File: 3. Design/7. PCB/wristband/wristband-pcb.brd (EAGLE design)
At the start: 160 x 100 mm, 44 parts, among them IC2 MAX16150AUT+T, IC5 STM32F051K6U6, Q1 2N7002NXAKR, Y2 FA-20H_16.0000MF12Z-AC3, Y3 FA-20H_16.0000MF12Z-AC3

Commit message: ADD|UPDT: Finished presentation
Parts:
- moved Y3 78.1 mm to (11.9, 13.0)
- moved BATT_HLD 67.4 mm to (13.1, 9.78), flipped to the bottom
- moved NRF24L01+ 63.8 mm to (12.7, 24.1)
- moved IC5 50.0 mm to (21.6, 22.9)
- moved PROG_IF 35.2 mm to (19.1, 40.9)
- moved MPU_6050_IF 29.7 mm to (29.8, 6.99)
- moved C11 16.5 mm to (42.8, 69.8)
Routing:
- net GND: track 0.00 -> 0.51 mm, vias 0 -> 10
- added copper zone on layer 16, net GND
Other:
- board size 160 x 100 mm -> 39.4 x 37.8 mm

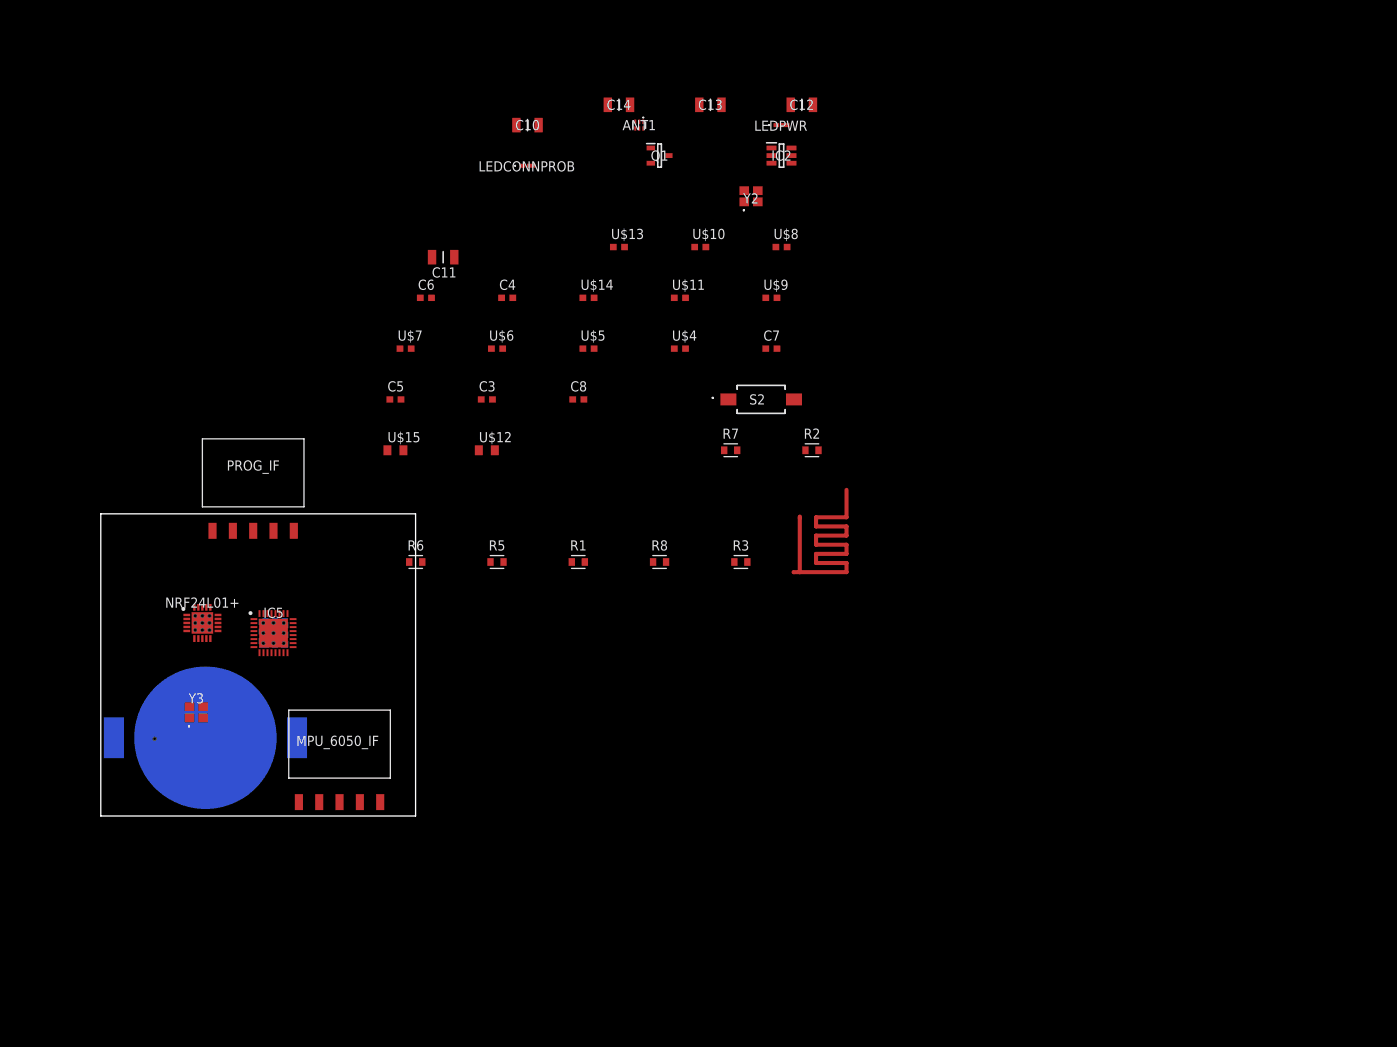
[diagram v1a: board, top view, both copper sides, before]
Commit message: UPDT: Added all work done on the Wristband PCB board so far
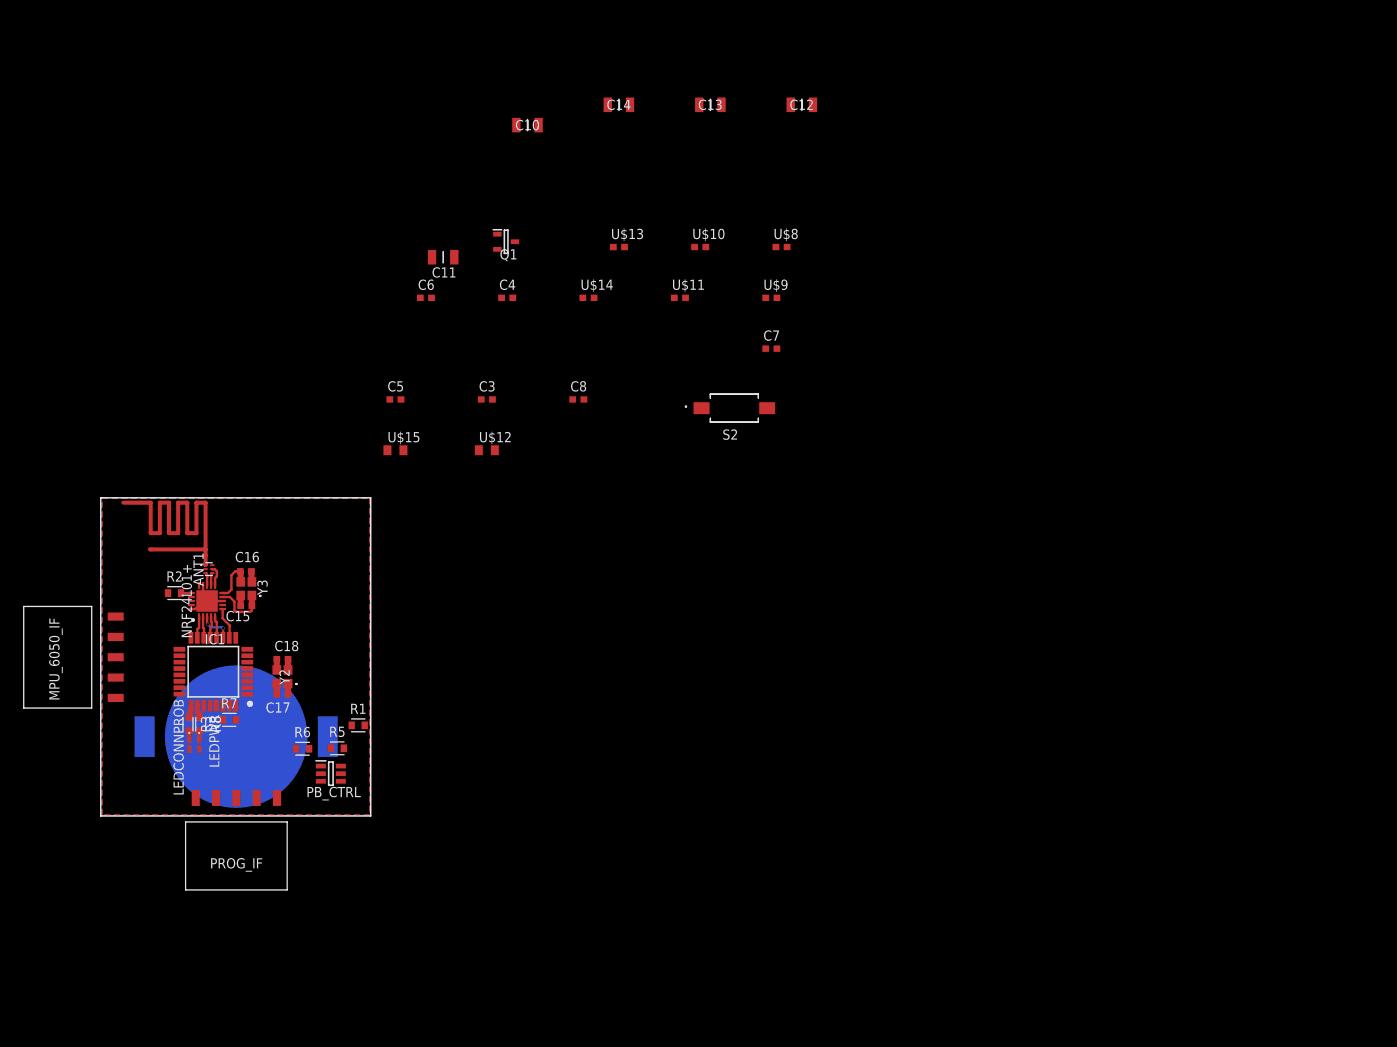
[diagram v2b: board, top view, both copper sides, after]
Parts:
- removed IC2: MAX16150AUT+T, MAX16150AUT+T:SOT95P280X145-6N
- removed IC5: STM32F051K6U6, STM32F051K6U6:QFN50P500X500X60-33N
- removed U$4, U$5, U$6, U$7: 22pF [0603], Nordic_nRF:RESC0603_L
- added C15, C16, C17, C18: 22pF [0603], Nordic_nRF:RESC0603_L
- added IC1: STM32F051K8T6, stm32f051k8t6:QFP80P900X900X160-32N
- added PB_CTRL: MAX16150AUT+T, MAX16150AUT+T:SOT95P280X145-6N
- moved LEDPWR 106.3 mm to (12.3, 8.84), turned to 270 degrees
- moved Y2 83.9 mm to (22.7, 17.4), turned to 90 degrees
- moved LEDCONNPROB 83.9 mm to (11.1, 8.84), turned to 270 degrees
- moved R2 81.7 mm to (9.22, 27.9)
- moved ANT1 77.3 mm to (13.5, 30.9), turned to 90 degrees
- moved U$2 73.3 mm to (13.1, 32.3), turned to 90 degrees
- moved R3 71.9 mm to (11.1, 11.5), turned to 270 degrees
- moved R7 71.2 mm to (16.1, 12.0)
- moved R8 61.0 mm to (12.3, 11.5), turned to 270 degrees
- moved PROG_IF 43.9 mm to (16.9, -2.99), turned to 180 degrees
- moved MPU_6050_IF 35.6 mm to (-3.38, 19.8), turned to 90 degrees
- moved R1 34.3 mm to (32.2, 11.3)
- moved R5 30.7 mm to (29.6, 8.46)
- moved R6 27.3 mm to (25.2, 8.41)
- moved Q1 22.0 mm to (50.7, 71.8)
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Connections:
- net GND: now also C15.2, C16.2, C17.2, C18.2, IC1.16, IC1.32, PB_CTRL.2; no longer IC2.2, IC5.33, U$4.2, U$5.2, U$6.2, U$7.2
- net LED_CONN_PROB: now also IC1.25; no longer IC5.26
- net LED_PWR: now also IC1.26; no longer IC5.27
- net MPU_6050_INT: now also IC1.27; no longer IC5.28
- net MPU_6050_SCL: now also IC1.28; no longer IC5.29
- net MPU_6050_SDA: now also IC1.29; no longer IC5.30
- net N$2: now also PB_CTRL.1; no longer IC2.1
- net N$4: now also IC1.30; no longer IC5.31
- net N$5: now also PB_CTRL.4; no longer IC2.4
- net NRF24L01_CE: now also IC1.15; no longer IC5.15
- net NRF24L01_CRYSTAL1: now also C16.1, Y3.3; no longer U$7.1, Y3.1
- net NRF24L01_CRYSTAL2: now also C15.1, Y3.1; no longer U$6.1, Y3.3
- net NRF24L01_CSN: now also IC1.14; no longer IC5.14
- net NRF24L01_IRQ: now also IC1.10; no longer IC5.16
- net NRF24L01_MISO: now also IC1.12; no longer IC5.12
- net NRF24L01_MOSI: now also IC1.13; no longer IC5.13
- net NRF24L01_SCK: now also IC1.11; no longer IC5.11
- net PWR_CLR: now also IC1.6, PB_CTRL.6; no longer IC2.6, IC5.6
- net PWR_INT: now also IC1.7, PB_CTRL.5; no longer IC2.5, IC5.7
- net STM32F051_CRYSTAL1: now also C17.1, IC1.2; no longer IC5.2, U$4.1
- net STM32F051_CRYSTAL2: now also C18.1, IC1.3; no longer IC5.3, U$5.1
- net SYS_NRST: now also IC1.4; no longer IC5.4
- net SYS_SWCLK: now also IC1.24; no longer IC5.24
- net SYS_SWDIO: now also IC1.23; no longer IC5.23
- net VCC_BATT: now also PB_CTRL.3; no longer IC2.3
- net VDD: now also IC1.1, IC1.17; no longer IC5.1, IC5.17
- net VDDA: now also IC1.5; no longer IC5.5
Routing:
- net GND: track 0.51 -> 11.8 mm, vias 10 -> 0
- net NRF24L01_CRYSTAL2: track 0.00 -> 6.99 mm
- net NRF24L01_CRYSTAL1: track 0.00 -> 5.72 mm
- net NRF24L01_SCK: track 0.00 -> 4.33 mm, vias 0 -> 2
- net NRF24L01_IRQ: track 0.00 -> 3.97 mm
- net NRF24L01_MOSI: track 0.00 -> 2.79 mm
- net NRF24L01_MISO: track 0.00 -> 2.78 mm
- net NRF24L01_CE: track 0.00 -> 2.74 mm
- net NRF24L01_CSN: track 0.00 -> 2.72 mm
- net VDDPA: track 0.00 -> 2.53 mm
- net ANT2: track 0.00 -> 1.62 mm
- net LED_CONN_PROB: track 0.00 -> 1.60 mm
- net LED_PWR: track 0.00 -> 1.60 mm
- net ANT1: track 0.00 -> 1.59 mm
- net STM32F051_CRYSTAL2: track 0.00 -> 1.36 mm
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- added copper zone on layer 1, net GND
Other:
- board size 39.4 x 37.8 mm -> 33.8 x 39.8 mm

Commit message: UPDT: PCB Wristband
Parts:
- removed U$10, U$13: 1uF [0603], Nordic_nRF:RESC0603_L
- removed U$12, U$15: 4.7nF [0805], Nordic_nRF:RESC0805_L
- added PS1: AP22814AW5-7, AP22814AW5-7:SOT95P285X130-5N
- added U$3, U$4: 4.7uF [0603], Nordic_nRF:RESC0603_L
- moved C12 93.1 mm to (24.6, 20.4), flipped to the bottom
- moved Q1 88.2 mm to (-7.67, 5.66)
- moved C13 83.8 mm to (24.6, 22.9), flipped to the bottom
- moved U$8 80.8 mm to (20.8, 22.1)
- moved S2 79.8 mm to (14.1, 4.85)
- moved U$11 78.2 mm to (6.65, 22.4), turned to 180 degrees
- moved U$9 76.8 mm to (20.8, 20.9)
- moved C10 76.7 mm to (24.6, 15.3), flipped to the bottom
- moved C14 75.2 mm to (24.6, 25.4), flipped to the bottom
- moved C7 74.3 mm to (18.2, 23.6)
- moved U$14 67.4 mm to (19.0, 12.0)
- moved C4 57.1 mm to (8.38, 26.5), turned to 180 degrees
- moved C11 55.2 mm to (24.6, 17.8), flipped to the bottom
- moved C3 48.8 mm to (8.38, 23.9), turned to 180 degrees
- moved C8 46.4 mm to (18.1, 31.7)
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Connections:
- new net IN: PS1.5
- new net OUT: PS1.1
- net GND: now also PS1.2, U$3.2, U$4.2; no longer U$10.2, U$12.2, U$13.2, U$15.2
- net VDD: now also U$3.1, U$4.1; no longer U$10.1, U$12.1, U$13.1, U$15.1
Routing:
- net VDD: track 0.00 -> 12.5 mm
- net N$2: track 0.00 -> 6.49 mm
- net DVDD: track 0.00 -> 4.48 mm
- net PWR_CLR: track 0.00 -> 4.29 mm
- net VDDA: track 0.00 -> 3.94 mm
- net VDDPA: track 2.53 -> 6.28 mm
- net N$5: track 0.00 -> 3.72 mm
- net PWR_INT: track 0.00 -> 2.27 mm
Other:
- board size 33.8 x 39.8 mm -> 27.7 x 39.8 mm

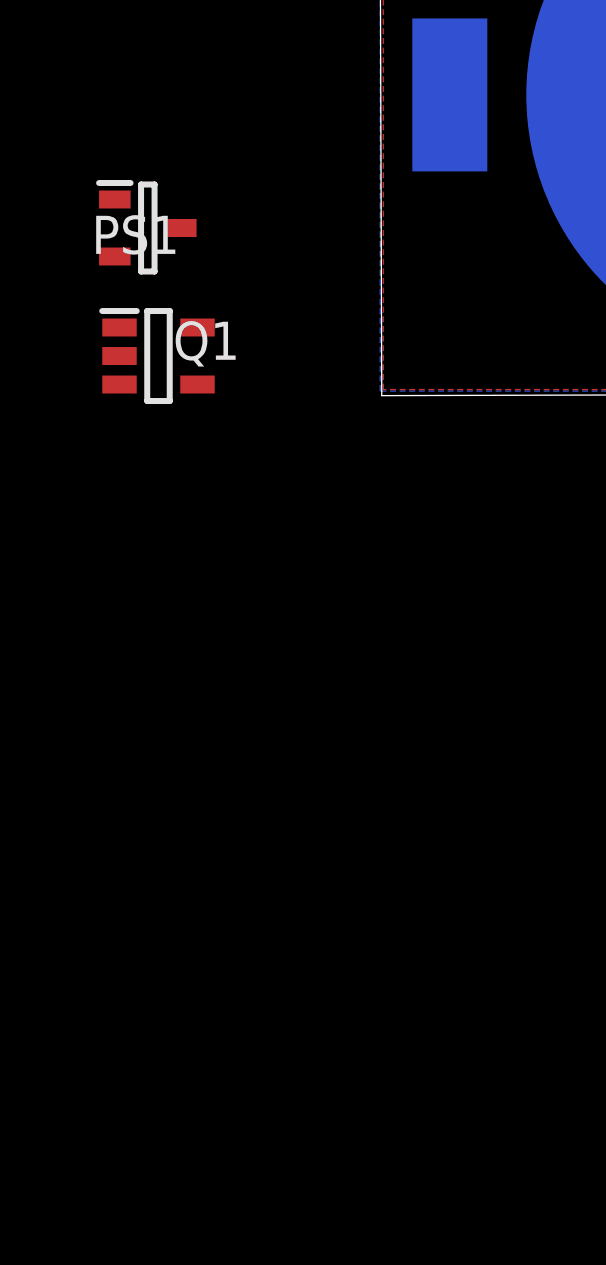
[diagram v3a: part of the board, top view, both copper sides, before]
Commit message: UPDT: Added Load Switch to Wristband PCB
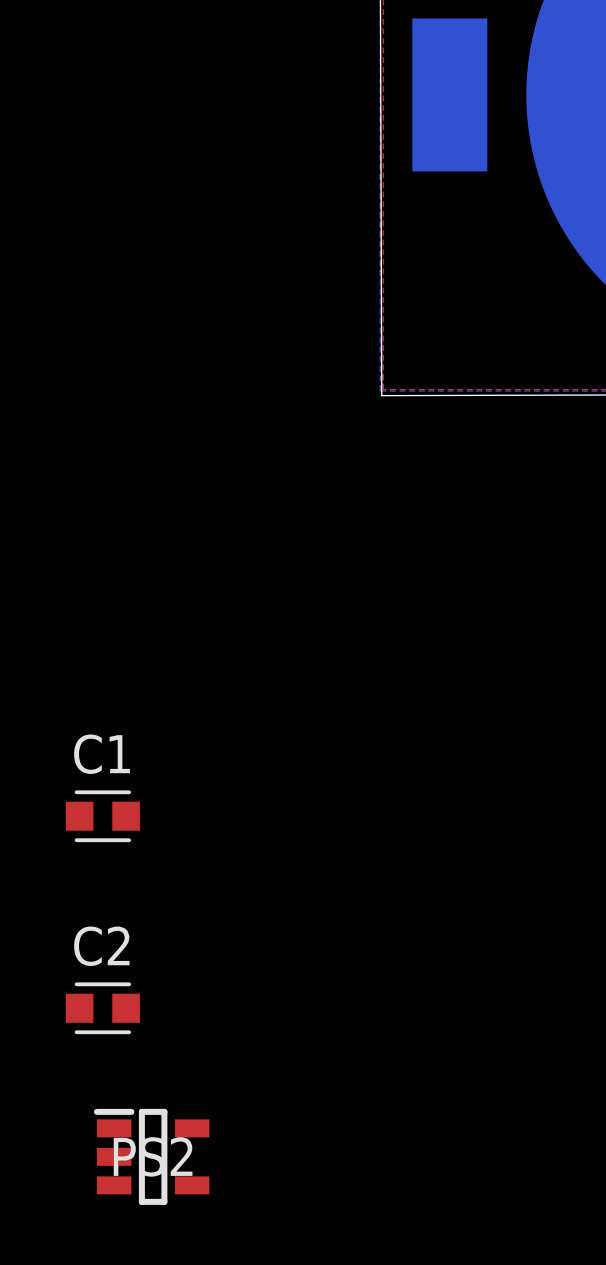
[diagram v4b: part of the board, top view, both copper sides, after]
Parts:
- removed PS1: AP22814AW5-7, AP22814AW5-7:SOT95P285X130-5N
- removed Q1: 2N7002NXAKR, 2N7002NXAKR:SOT95P230X110-3N
- added C1, C2: 100n [0603], Capacitor:CAPC1608X85
- added PS2: AP22814AW5-7, AP22814AW5-7:SOT95P285X130-5N
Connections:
- removed net IN: PS1.5
- removed net OUT: PS1.1
- new net FLG: PS2.3
- net GND: now also C1.2, C2.2, PS2.2; no longer PS1.2
- net N$5: now also PS2.4; no longer Q1.1
- net VCC_BATT: now also C2.1, PS2.5; no longer Q1.3
- net VDD: now also C1.1, PS2.1; no longer Q1.2

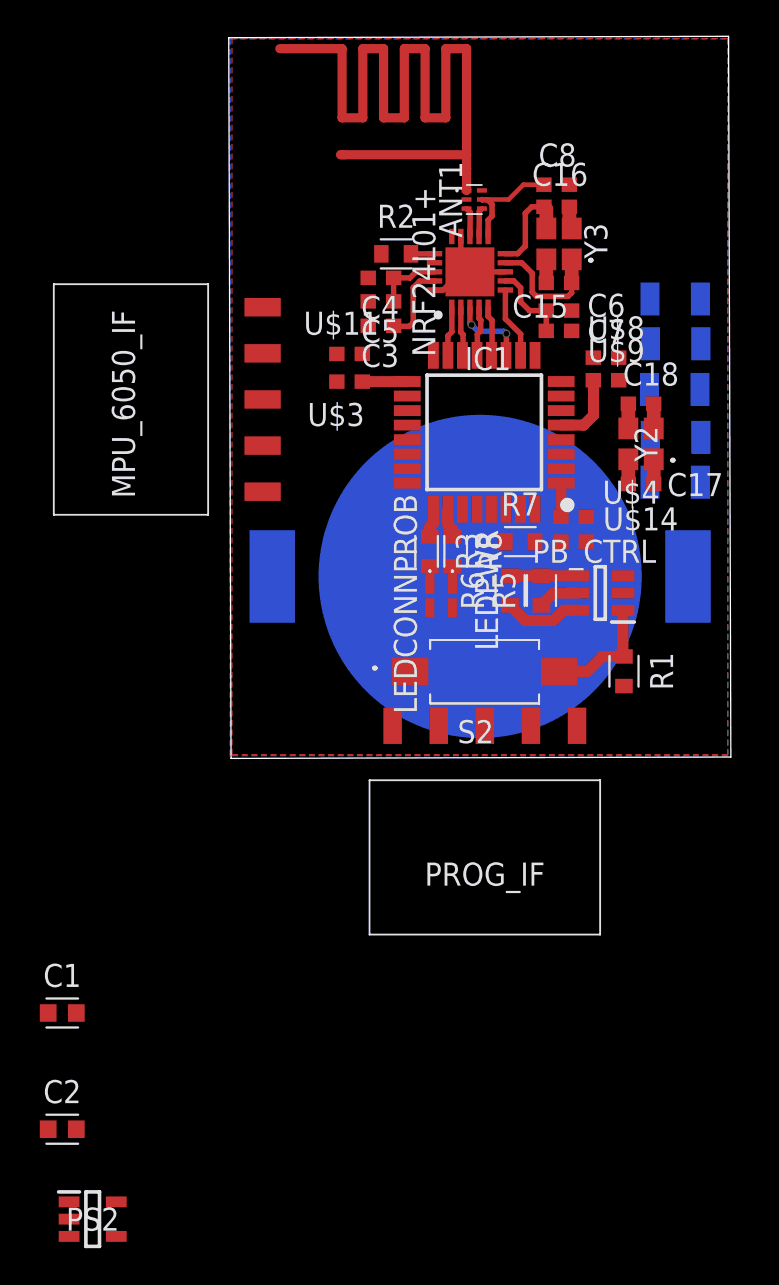
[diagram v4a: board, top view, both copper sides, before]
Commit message: UPDT: Updated wristband PCB design with new connections and slightly different layout
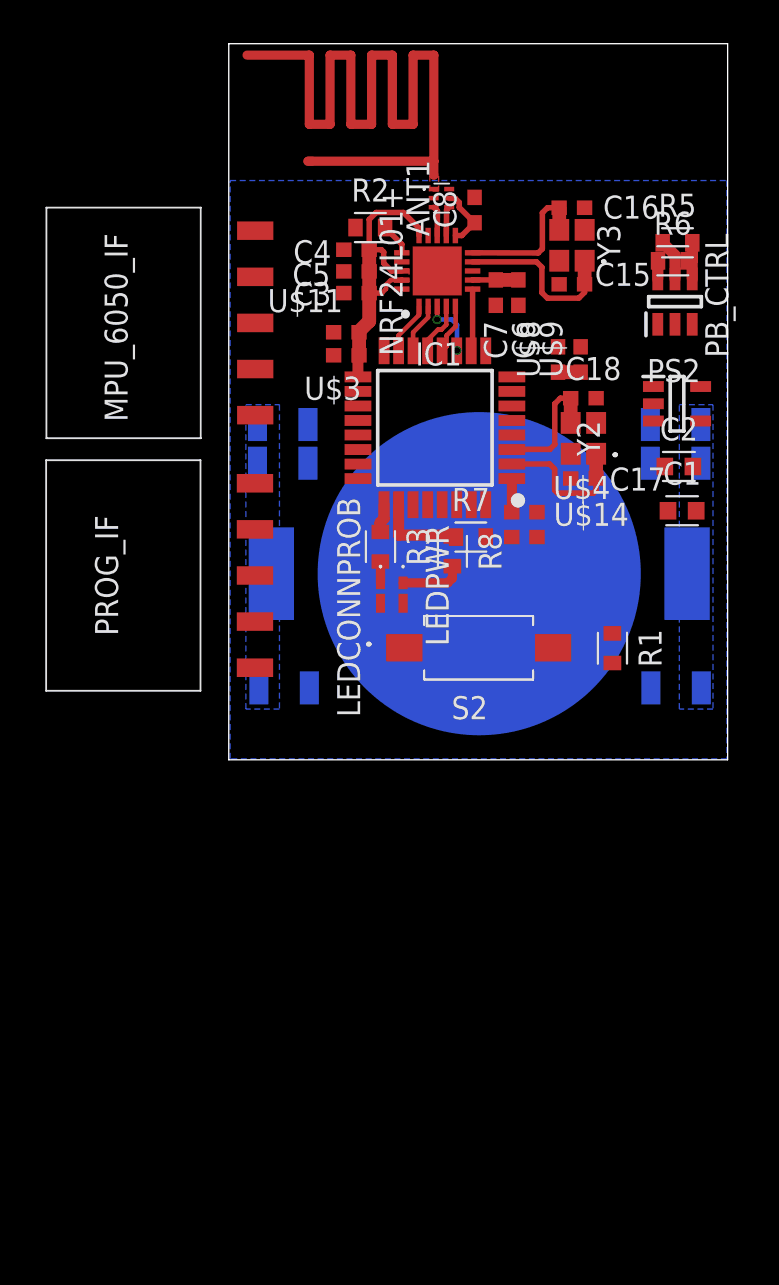
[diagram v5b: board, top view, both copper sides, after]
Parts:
- added C9: 22nF [1206], CL31B226KPHNNNE:CAPC3216X180N
- moved PS2 55.2 mm to (24.7, 19.6)
- moved C2 49.9 mm to (24.8, 16.2)
- moved C1 43.9 mm to (25.0, 13.7)
- moved C14 22.7 mm to (2.97, 18.5), turned to 180 degrees
- moved C13 22.6 mm to (2.97, 16.3), turned to 180 degrees
- moved PROG_IF 22.4 mm to (-3.81, 10.2), turned to 90 degrees
- moved R5 20.6 mm to (24.7, 28.5), turned to 0 degrees
- moved R6 20.3 mm to (24.5, 27.5), turned to 0 degrees
- moved PB_CTRL 16.6 mm to (24.6, 25.2), turned to 90 degrees
- moved C10 11.3 mm to (24.6, 3.96)
- moved C8 4.73 mm to (13.5, 30.3), turned to 90 degrees
- moved MPU_6050_IF 4.24 mm to (-3.79, 24.1)
- moved C7 4.07 mm to (14.7, 25.7), turned to 270 degrees
- moved C17 3.19 mm to (19.5, 15.5)
- moved C18 3.19 mm to (19.5, 19.9)
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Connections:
- removed net DVDD: C3.1, NRF24L01+.19
- net GND: now also C9.2
- net VCC_BATT: now also C10.1, C9.1
- net VDD: now also C3.1, NRF24L01+.19
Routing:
- net GND: track 11.7 -> 0.00 mm
- net VDD: track 12.5 -> 21.9 mm
- net STM32F051_CRYSTAL1: track 1.36 -> 8.06 mm
- net N$2: track 6.49 -> 0.08 mm
- net STM32F051_CRYSTAL2: track 1.36 -> 7.08 mm
- net DVDD: track 4.48 -> 0.00 mm
- net PWR_CLR: track 4.29 -> 1.01 mm
- net LED_PWR: track 1.60 -> 4.72 mm
- net VDDPA: track 6.28 -> 3.46 mm
- net NRF24L01_CRYSTAL2: track 6.95 -> 9.69 mm
- net VDDA: track 3.94 -> 1.24 mm
- net NRF24L01_CRYSTAL1: track 5.50 -> 8.18 mm
- net N$6: track 1.18 -> 3.49 mm
- net N$1: track 1.20 -> 0.00 mm
- net NRF24L01_SCK: track 4.33 -> 3.40 mm
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- added copper zone on layer 1, net N$1
- added copper zone on layer 16, net VCC_BATT
- added copper zone on layer 1, net VDD
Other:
- board size 27.7 x 39.8 mm -> 27.5 x 39.4 mm
